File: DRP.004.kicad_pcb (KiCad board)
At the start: 2 copper layers, 53.4 x 26.8 mm, 73 parts, among them J1 Conn_01x03_Pin, J2 USB_C_Receptacle_PowerOnly_6P, J3 Conn_01x03_Pin, J4 Conn_01x05_Pin, J5 Conn_01x03_Pin, J6 Conn_01x03_Pin, Q1 2N7002, Q2 2N7002, Q3 DTC143Z, Q4 DTC143Z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

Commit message: Buffed MOSFETs - Changed Q1,Q2 to AO3400 - Changed Q4 to DMG1012T
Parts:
- Q1, Q2: value 2N7002 -> AO3400
- Q4: value DTC143Z -> DMG1012T

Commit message: Adjusted stencil for custom jig
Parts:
- added FID1: Fiducial, Fiducial:Fiducial_0.5mm_Mask1.5mm, F.Cu at (116.8, 47.5)
- added FID2: Fiducial, Fiducial:Fiducial_0.5mm_Mask1.5mm, F.Cu at (150.4, 68.7)
- added FID3: Fiducial, Fiducial:Fiducial_0.5mm_Mask1.5mm, F.Cu at (109.8, 70.3)
- added FID4: Fiducial, Fiducial:Fiducial_0.5mm_Mask1.5mm, F.Cu at (159.2, 57.3)
- moved C11 5.92 mm to (150.7, 61.5), turned to -90 degrees
- moved R22 1.07 mm to (144.1, 66.4)
- moved Q4 0.79 mm to (143.8, 68.3)
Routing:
- net /power/power_control/SWITCH: track 39.3 -> 37.4 mm
- net +3V3: track 76.5 -> 75.4 mm
- net Net-(J6-Pin_1): track 6.88 -> 7.61 mm
- net EN_LDR: track 5.36 -> 6.00 mm
- net GND: vias 378 -> 380

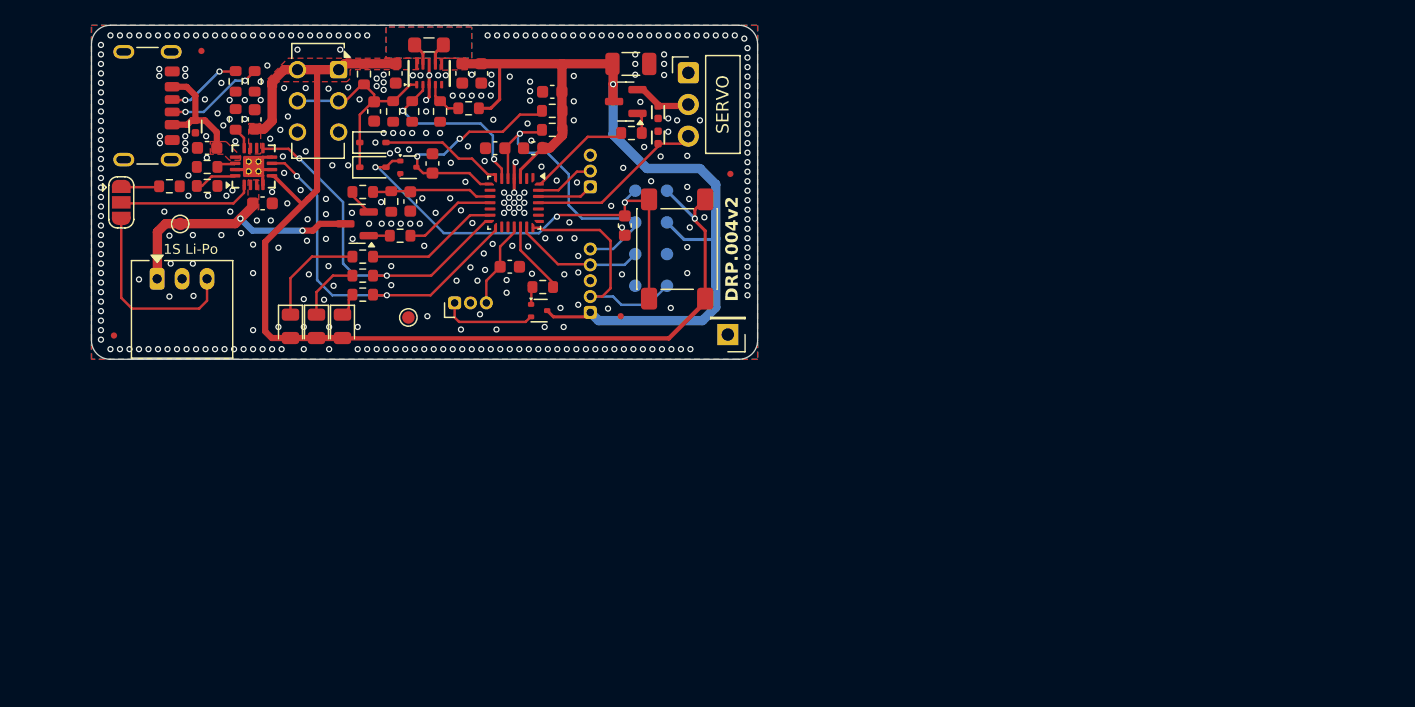
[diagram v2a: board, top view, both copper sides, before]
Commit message: Rough placment of components for v3
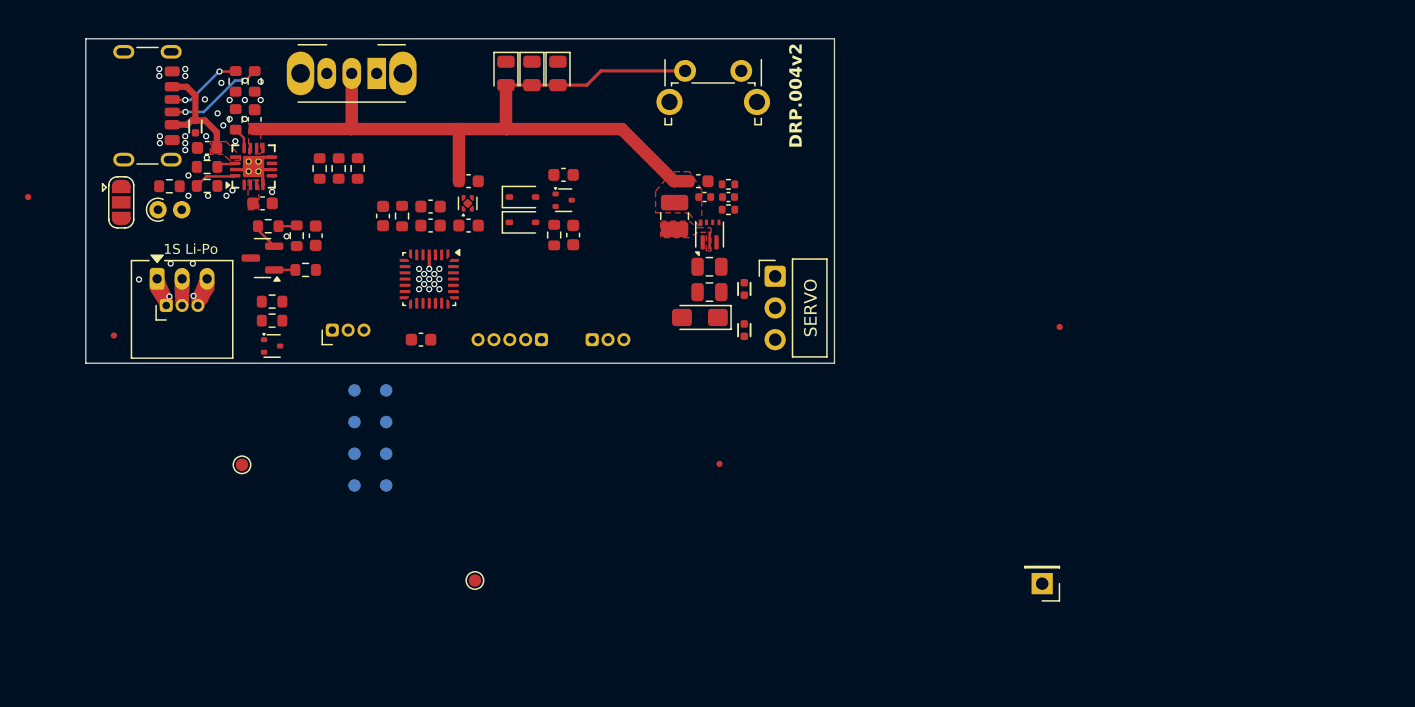
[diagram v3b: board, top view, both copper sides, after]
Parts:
- removed Q1: AO3400, Package_TO_SOT_SMD:SOT-23
- removed R12, R7, R8: 10k, Resistor_SMD:R_0603_1608Metric
- removed SW1: SW_Slide_DPDT, Button_Switch_THT:SW_CK_JS202011CQN_DPDT_Straight
- removed U7: TPD1E10B06DPYR, TPD1E10B06DPYR:X1SON-2_L1.0-W0.6-P0.65-BI
- added C17: 1uF, Capacitor_SMD:C_0603_1608Metric, F.Cu at (138.2, 61.5)
- added C18: 10pF, Capacitor_SMD:C_0402_1005Metric, F.Cu at (159.0, 59.2)
- added C5: 1uF, Capacitor_SMD:C_0603_1608Metric, F.Cu at (138.2, 57.9)
- added SW3: SW_SPDT, Button_Switch_THT:SW_Slide_SPDT_Angled_CK_OS102011MA1Q, F.Cu at (130.8, 49.3)
- added TH1: 10k NTC, Resistor_THT:R_Axial_DIN0204_L3.6mm_D1.6mm_P1.90mm_Vertical, F.Cu at (113.3, 60.2)
- added U3: AP7343D-18FS4, Muffin_SMD:X2SON-4_1x1mm_P0.65mm, F.Cu at (138.1, 59.7)
- added U8: TPD1E10B06DPYR, Muffin_SMD:X1SON-2_L1.0-W0.6-P0.65-BI, F.Cu at (160.3, 69.8)
- C15: footprint Capacitor_SMD:C_1206_3216Metric -> Capacitor_Tantalum_SMD:CP_EIA-3216-18_Kemet-A_HandSolder
- C3, C4: footprint Capacitor_SMD:C_0603_1608Metric -> Capacitor_SMD:C_0805_2012Metric
- C7: value 0.1uF -> 100nF; footprint Capacitor_SMD:C_0603_1608Metric -> Capacitor_SMD:C_0402_1005Metric
- J1: value Conn_01x03_Pin -> Batt_conn_3p; footprint conn:JST_PH_S3B-PH-K_1x03_P2.00mm_Horizontal -> Muffin_CONNECTOR_THT:BATTERY_P2+P1.27mm_Horizontal
- L1: value 0.47uh -> 1.0uh; footprint Inductor_SMD:L_0805_2012Metric_Pad1.05x1.20mm_HandSolder -> Inductor_SMD:L_1008_2520Metric
- Q4: footprint SOT-523:SOT-523 -> Muffin_SMD:SOT-523
- R1: value 0 -> 100k
- R16: value 10k -> 3.3k
- R2: value 180k -> 100k; footprint Resistor_SMD:R_0603_1608Metric -> Resistor_SMD:R_0402_1005Metric
- R6: value 33k -> 750k; footprint Resistor_SMD:R_0603_1608Metric -> Resistor_SMD:R_0402_1005Metric
- SW2: footprint SWITCHES:SW_SPST_PTS645 -> Button_Switch_THT:SW_Tactile_SPST_Angled_PTS645Vx58-2LFS
- U2: value TPS63802DLAR -> TPD1E10B06DPYR; footprint TPS63802:DLA0010A -> Muffin_SMD:X1SON-2_L1.0-W0.6-P0.65-BI
- U4: footprint TPD1E10B06DPYR:X1SON-2_L1.0-W0.6-P0.65-BI -> Muffin_SMD:X1SON-2_L1.0-W0.6-P0.65-BI
- U5: value TPD1E10B06DPYR -> TPS61022RWUR; footprint TPD1E10B06DPYR:X1SON-2_L1.0-W0.6-P0.65-BI -> Muffin_SMD:RWU0007A
- U6: footprint STM32G031G8Ux:QFN-28_4x4mm_P0.5mm -> Muffin_SMD:QFN-28_4x4mm_P0.5mm
- moved U4 37.1 mm to (116.3, 53.5), turned to -90 degrees
- moved TP6 32.1 mm to (184.2, 90.2)
- moved U2 30.6 mm to (160.3, 66.5)
- moved D5 29.5 mm to (145.3, 49.3)
- moved FID4 29.1 mm to (185.5, 69.6)
- moved TP9 27.6 mm to (131.6, 82.3)
- moved TP1 27.6 mm to (131.6, 74.7)
- moved TP8 27.6 mm to (131.6, 79.8)
- moved TP2 27.6 mm to (131.6, 77.2)
- moved TP10 27.6 mm to (129.0, 82.3)
- moved TP11 27.6 mm to (129.0, 74.7)
- moved TP4 27.6 mm to (129.0, 79.8)
- moved TP5 27.6 mm to (129.0, 77.2)
- moved C7 27.4 mm to (157.1, 59.2), turned to 180 degrees
- moved C3 26.5 mm to (157.5, 66.8), turned to 180 degrees
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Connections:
- net /power/power_control/SWITCH renamed /control/SWITCH
- C12 pad 1: +3V3 -> +1V8
- C13 pad 1: +3V3 -> +1V8
- C15 pad 1: +3V3 -> +5V5
- C3 pad 1: +3V3 -> +5V5
- C4 pad 1: +3V3 -> +5V5
- C7 pad 1: EN_SYS -> GND
- C7 pad 2: GND -> VSYS
- J3 pad 2: Net-(J3-Pin_2) -> +5V5
- J3 pad 3: SERWO_PWM -> SERVO_PWM
- J4 pad 1: +3V3 -> +1V8
- L1 pad 1: Net-(U2-L1) -> VSYS
- L1 pad 2: Net-(U2-L2) -> Net-(U5-SW)
- Q4 pad 3: +3V3 -> +1V8
- R1 pad 1: EN_SYS -> Net-(Q4-G)
- R1 pad 2: VSYS -> GND
- R18 pad 2: +3V3 -> +1V8
- R19 pad 2: +3V3 -> +1V8
- R2 pad 1: +3V3 -> Net-(U5-FB)
- R2 pad 2: /power/DC-DC_FB -> GND
- R6 pad 1: /power/DC-DC_FB -> +5V5
- R6 pad 2: GND -> Net-(U5-FB)
- TP2 pad 1: +3V3 -> +5V5
- U2 pad 1: EN_SYS -> +5V5
- U2 pad 2: MODE_SW -> GND
- U4 pad 1: SERWO_PWM -> VBUS
- U5 pad 2: Net-(J3-Pin_2) -> Net-(U5-SW)
- U6 pad 11: EN_LOAD_BATT -> unconnected-(U6-PA5-Pad11)
- U6 pad 14: CHRG -> PGOOD
- U6 pad 15: PGOOD -> CHRG
- U6 pad 16: unconnected-(U6-PA8-Pad16) -> EN_LOAD_BATT
- U6 pad 18: ADC_LDR -> EN_LDR
- U6 pad 19: EN_LDR -> ADC_LDR
- U6 pad 25: SERWO_PWM -> SERVO_PWM
- U6 pad 3: +3V3 -> +1V8
- U6 pad 6: MODE_SW -> unconnected-(U6-PA0-Pad6)
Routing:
- net +3V3: track 75.4 -> 0.00 mm, vias 1 -> 0
- net /control/SWITCH: track 37.4 -> 0.05 mm, vias 3 -> 0
- net PGOOD: track 29.7 -> 0.00 mm, vias 2 -> 0
- net CHRG: track 28.2 -> 0.00 mm, vias 2 -> 0
- net VSYS: track 91.4 -> 63.7 mm, vias 1 -> 0
- net NRST: track 25.2 -> 0.36 mm, vias 1 -> 0
- net +BATT: track 21.5 -> 0.00 mm, vias 2 -> 0
- net SWCLK: track 19.5 -> 0.05 mm
- net ON_DETECT: track 18.8 -> 0.00 mm, vias 2 -> 0
- net EN_SYS: track 17.4 -> 0.00 mm
- net MODE_SW: track 14.6 -> 0.00 mm, vias 2 -> 0
- net SERWO_PWM: track 14.3 -> 0.00 mm
- net Net-(J1-TS): track 15.7 -> 2.74 mm
- net TS: track 10.9 -> 0.00 mm
- net LED_RED: track 10.8 -> 0.00 mm
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- added copper zone on F.Cu, net Net-(U5-SW)
- removed copper zone on F.Cu, net +3V3
- removed copper zone on B.Cu, net GND
- removed copper zone on F.Cu, net GND
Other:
- board size 53.4 x 26.8 mm -> 60 x 26 mm

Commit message: Routed v3
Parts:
- removed C15: 47uF, Capacitor_Tantalum_SMD:CP_EIA-3216-18_Kemet-A_HandSolder
- removed U3: AP7343D-18FS4, Muffin_SMD:X2SON-4_1x1mm_P0.65mm
- added U7: AP2112K-1.8, Package_TO_SOT_SMD:SOT-23-5, F.Cu at (138.2, 58.2)
- #G1: moved to F.Cu
- C2: footprint Capacitor_SMD:C_0603_1608Metric -> Capacitor_SMD:C_0805_2012Metric
- C7: value 100nF -> 0.1uF; footprint Capacitor_SMD:C_0402_1005Metric -> Capacitor_SMD:C_0603_1608Metric
- moved TP6 48.0 mm to (160.7, 48.3), turned to 0 degrees
- moved FID4 42.8 mm to (146.6, 51.8)
- moved TP7 30.2 mm to (153.9, 63.9)
- moved TP11 27.6 mm to (148.9, 55.5)
- moved #G1 26.6 mm to (148.7, 64.3), turned to 90 degrees
- moved TP10 21.9 mm to (145.9, 68.3)
- moved C7 21.8 mm to (135.5, 56.1), turned to -90 degrees
- moved TP2 20.4 mm to (150.0, 68.3), turned to 90 degrees
- moved TP9 18.6 mm to (143.9, 68.3)
- moved R23 18.6 mm to (146.1, 48.9), turned to -90 degrees
- moved TP3 18.2 mm to (116.2, 62.9)
- moved TP1 17.6 mm to (148.0, 68.3), turned to 90 degrees
- moved R21 16.8 mm to (142.5, 48.9), turned to -90 degrees
- moved TP4 15.7 mm to (139.8, 68.3)
- moved TP8 15.4 mm to (141.9, 68.3)
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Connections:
- net Net-(U5-FB) renamed /power/BOOST_FB
- net Net-(U5-SW) renamed /power/BOOST_SW
- C7 pad 2: VSYS -> EN_SYS
- D3 pad 1: Net-(D3-K) -> CHRG
- D3 pad 2: VSYS -> Net-(D3-A)
- D4 pad 1: Net-(D4-K) -> PGOOD
- D4 pad 2: VSYS -> Net-(D4-A)
- D5 pad 1: Net-(D5-K) -> LED_RED
- D5 pad 2: VSYS -> Net-(D5-A)
- R20 pad 1: CHRG -> Net-(D3-A)
- R20 pad 2: Net-(D3-K) -> VSYS
- R21 pad 1: PGOOD -> Net-(D4-A)
- R21 pad 2: Net-(D4-K) -> VSYS
- R23 pad 1: LED_RED -> Net-(D5-A)
- R23 pad 2: Net-(D5-K) -> VSYS
- TP1 pad 1: VSYS -> USART_TX
- TP10 pad 1: GND -> +1V8
- TP2 pad 1: +5V5 -> USART_RX
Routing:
- net +1V8: track 0.00 -> 53.5 mm, vias 0 -> 2
- net PGOOD: track 0.00 -> 34.2 mm, vias 0 -> 3
- net CHRG: track 0.00 -> 34.0 mm, vias 0 -> 3
- net SERVO_PWM: track 0.00 -> 33.0 mm, vias 0 -> 1
- net EN_SERVO: track 0.00 -> 31.0 mm, vias 0 -> 2
- net LED_RED: track 0.00 -> 27.5 mm, vias 0 -> 2
- net GND: track 8.58 -> 35.2 mm, vias 47 -> 88
- net EN_SYS: track 0.00 -> 23.6 mm, vias 0 -> 3
- net /control/SWITCH: track 0.05 -> 21.6 mm, vias 0 -> 1
- net USART_RX: track 0.00 -> 21.5 mm, vias 0 -> 1
- net ON_DETECT: track 0.00 -> 21.4 mm, vias 0 -> 2
- net ON_LATCH: track 0.00 -> 21.1 mm, vias 0 -> 2
- net USART_TX: track 0.00 -> 18.4 mm, vias 0 -> 1
- net NRST: track 0.36 -> 18.3 mm, vias 0 -> 1
- net +BATT: track 0.00 -> 17.5 mm
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- added copper zone on F.Cu, net +5V5
- added copper zone on B.Cu, net GND
- added copper zone on F.Cu, net GND
- added copper zone on In1.Cu, net GND
- added copper zone on In2.Cu, net GND
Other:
- board size 60 x 26 mm -> 55 x 27 mm
- copper layers 2 -> 4
- board text removed: "${2767fded-6c01-4ebd-83f7-0d2d1d7f05a7:SHORT_NET_NAME(1)} ${967ac194-9e53-4776-ae55-413b2efe6499:SHORT_NET_NAME(1)} ${da77c859-c5c3-4d9d-8514-6326ea20721f:SHORT_NET_NAME(1)} ${6ce6847d-f19f-43e2-bd95-286de52f06d8:SHORT_NET_NAME(1)}"
- board text removed: "${5c34ef5f-fa85-4952-b4f7-771e512ace45:SHORT_NET_NAME(1)} ${6b144688-801a-4334-acce-3b3506989d76:SHORT_NET_NAME(1)} ${4eff0c75-f831-4b6a-967d-1ccbdd22f45d:SHORT_NET_NAME(1)} ${c61ffe12-5a26-4d62-b70e-33fc13e1cee8:SHORT_NET_NAME(1)}"

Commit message: Finished v3
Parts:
- J6: footprint conn:PinHeader_1x03_P1.27mm_Vertical -> Muffin_CONNECTOR_THT:Connector_JST_1x03_P1.27mm
- moved #G1 2.09 mm to (146.7, 64.8), turned to 0 degrees
- moved C3 0.18 mm to (157.7, 65.0)
- moved C4 0.18 mm to (157.7, 63.0)
- moved J6 0.10 mm to (128.5, 68.7)
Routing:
- net SERVO_PWM: track 33.0 -> 26.5 mm
- net GND: track 35.2 -> 32.9 mm, vias 88 -> 177
- net CHRG: track 34.0 -> 35.7 mm
- net LED_RED: track 27.5 -> 29.1 mm
- net PGOOD: track 34.2 -> 35.8 mm
- net EN_SERVO: track 31.0 -> 32.1 mm
- net ON_DETECT: track 21.4 -> 20.8 mm
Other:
- board text added: "0.2000 mm / 0.1500 mm"
- board text added: "0.2500 mm"
- board text added: "1.6000 mm"
- board text added: "4"
- board text added: "55.0000 mm x 27.0000 mm"
- board text added: "BOARD CHARACTERISTICS"
- board text added: "BTN"
- board text added: "Board Thickness:"
- board text added: "Board overall dimensions:"
- board text added: "CHG"
- board text added: "Castellated pads:"
- board text added: "Copper Finish:"
- board text added: "Copper Layer Count:"
- board text added: "ENIG"
- board text added: "Edge card connectors:"
- board text added: "Impedance Control:"
- board text added: "LDR"
- board text added: "Min hole diameter:"
- board text added: "Min track/spacing:"
- board text added: "No"
- board text added: "ON/OFF"
- board text added: "PG"
- board text added: "Plated Board Edge:"
- board text added: "SYS"

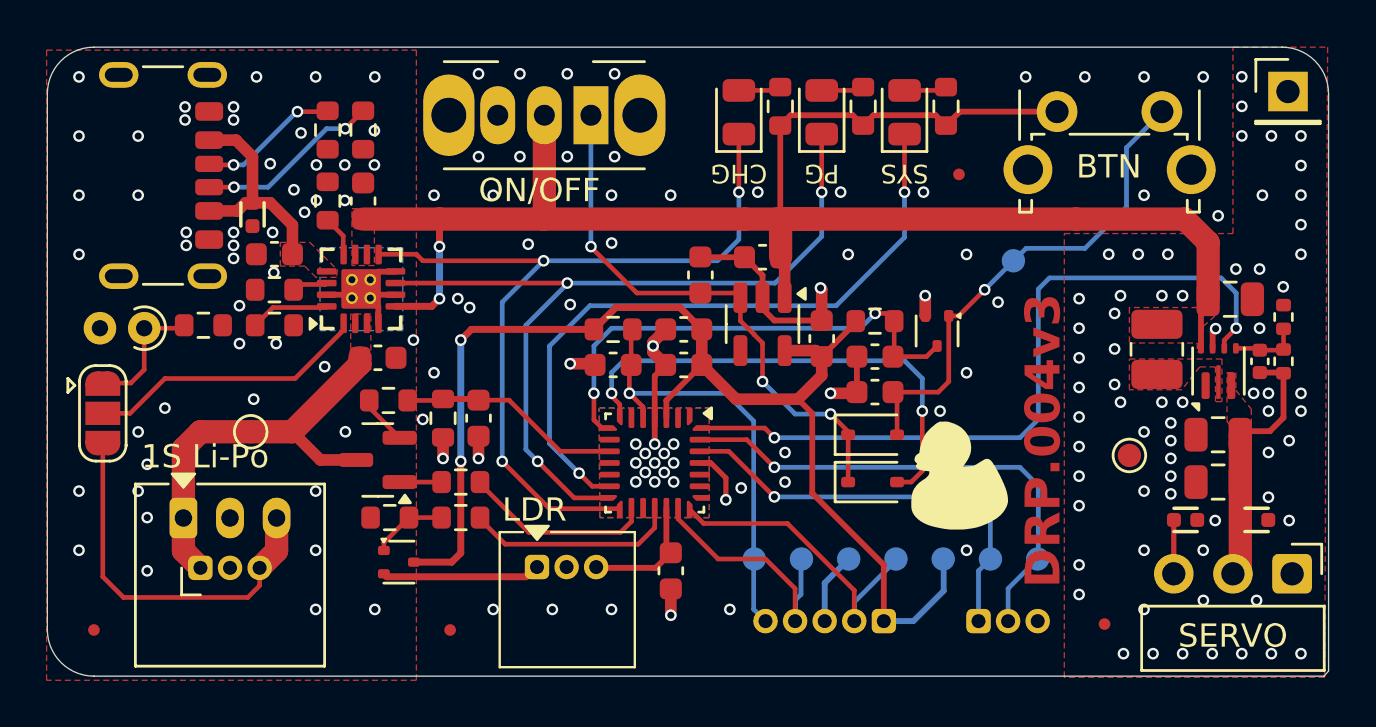
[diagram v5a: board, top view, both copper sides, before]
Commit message: Moved servo logic to 5v
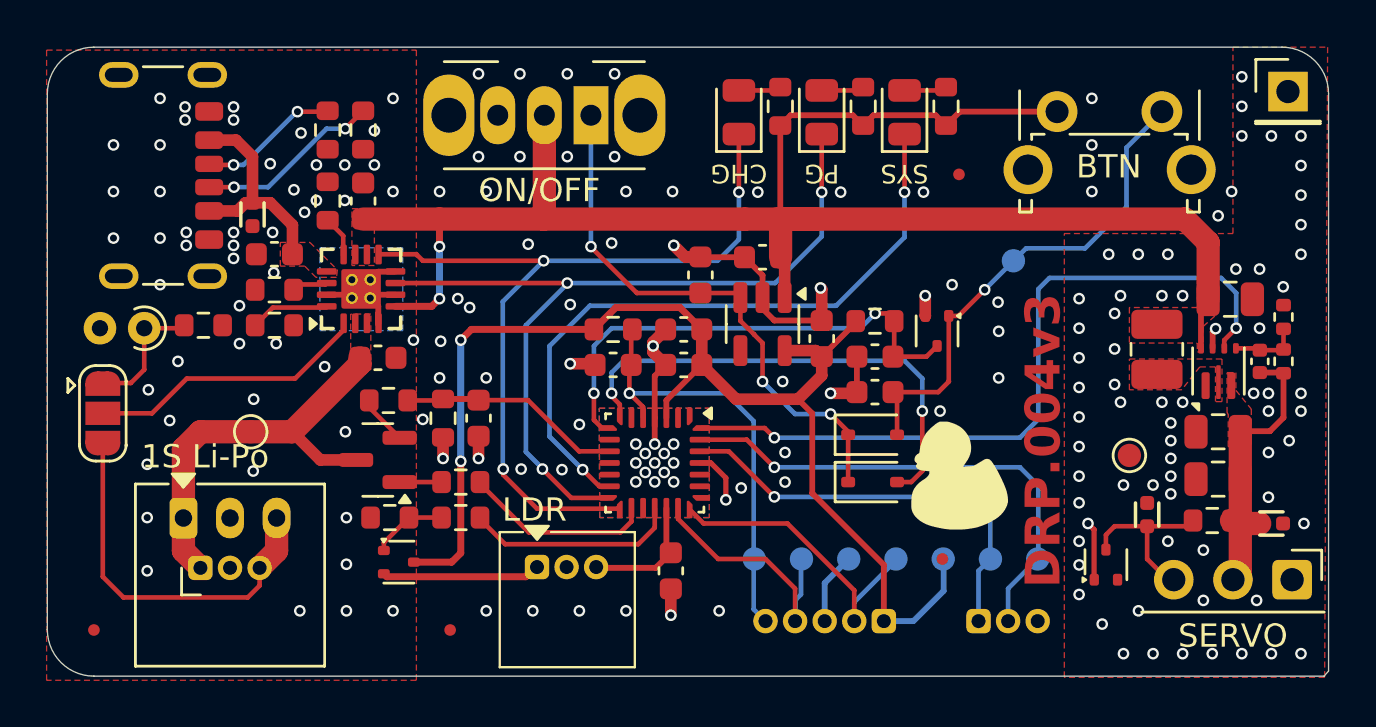
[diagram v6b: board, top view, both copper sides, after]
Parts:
- removed U8: TPD1E10B06DPYR, Muffin_SMD:X1SON-2_L1.0-W0.6-P0.65-BI
- added Q1: DTC143Z, SOT-523:SOT-523, F.Cu at (152.9, 68.6)
- added R7: 5.1k, Resistor_SMD:R_0603_1608Metric, F.Cu at (157.5, 66.7)
- added U3: TPD1E10B06DPYR, Muffin_SMD:X1SON-2_L1.0-W0.6-P0.65-BI, F.Cu at (154.7, 66.4)
- J3: footprint conn:PinHeader_1x03_P2.54mm_Horizontal -> Muffin_CONNECTOR_THT:PinHeader_1x03_P2.54mm_Horizontal
- moved FID2 7.50 mm to (145.9, 68.3)
- moved U2 0.65 mm to (160.0, 66.8)
- moved J3 0.25 mm to (160.9, 69.2)
- moved C3 0.13 mm to (157.7, 64.9)
- moved C4 0.13 mm to (157.7, 62.9)
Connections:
- J3 pad 3: SERVO_PWM -> Net-(J3-Pin_3)
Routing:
- net Net-(J3-Pin_3): track 0.00 -> 6.94 mm
- net SERVO_PWM: track 26.5 -> 20.8 mm, vias 1 -> 2
- net +5V5: track 10.9 -> 12.8 mm
- net GND: track 32.9 -> 34.2 mm, vias 177 -> 184
